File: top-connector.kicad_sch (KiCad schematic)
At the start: 6 parts, among them J1 Compute-Module-4_Plug_Connect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, Q2 DMG1012T-7

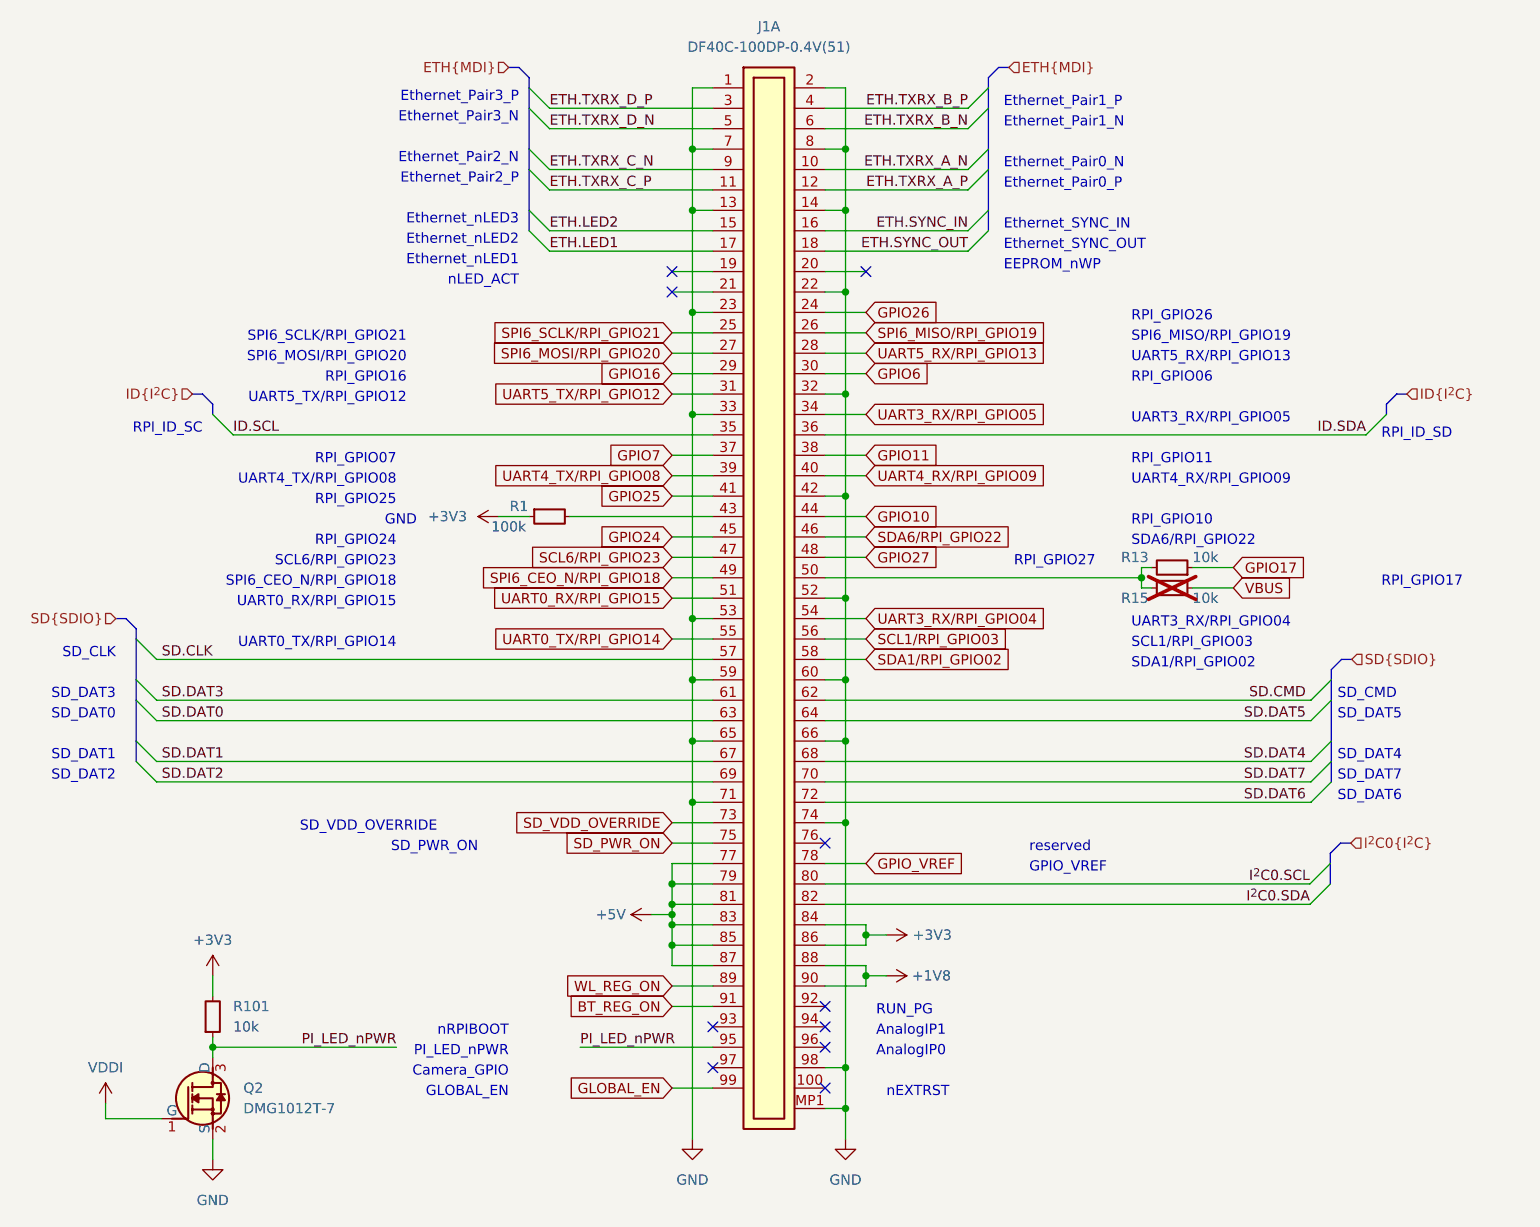
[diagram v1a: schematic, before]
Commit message: [#59450] Remove custom CM4 connector, add CM4 outline with regular DF40C-100DP-0.4V(51) connectors
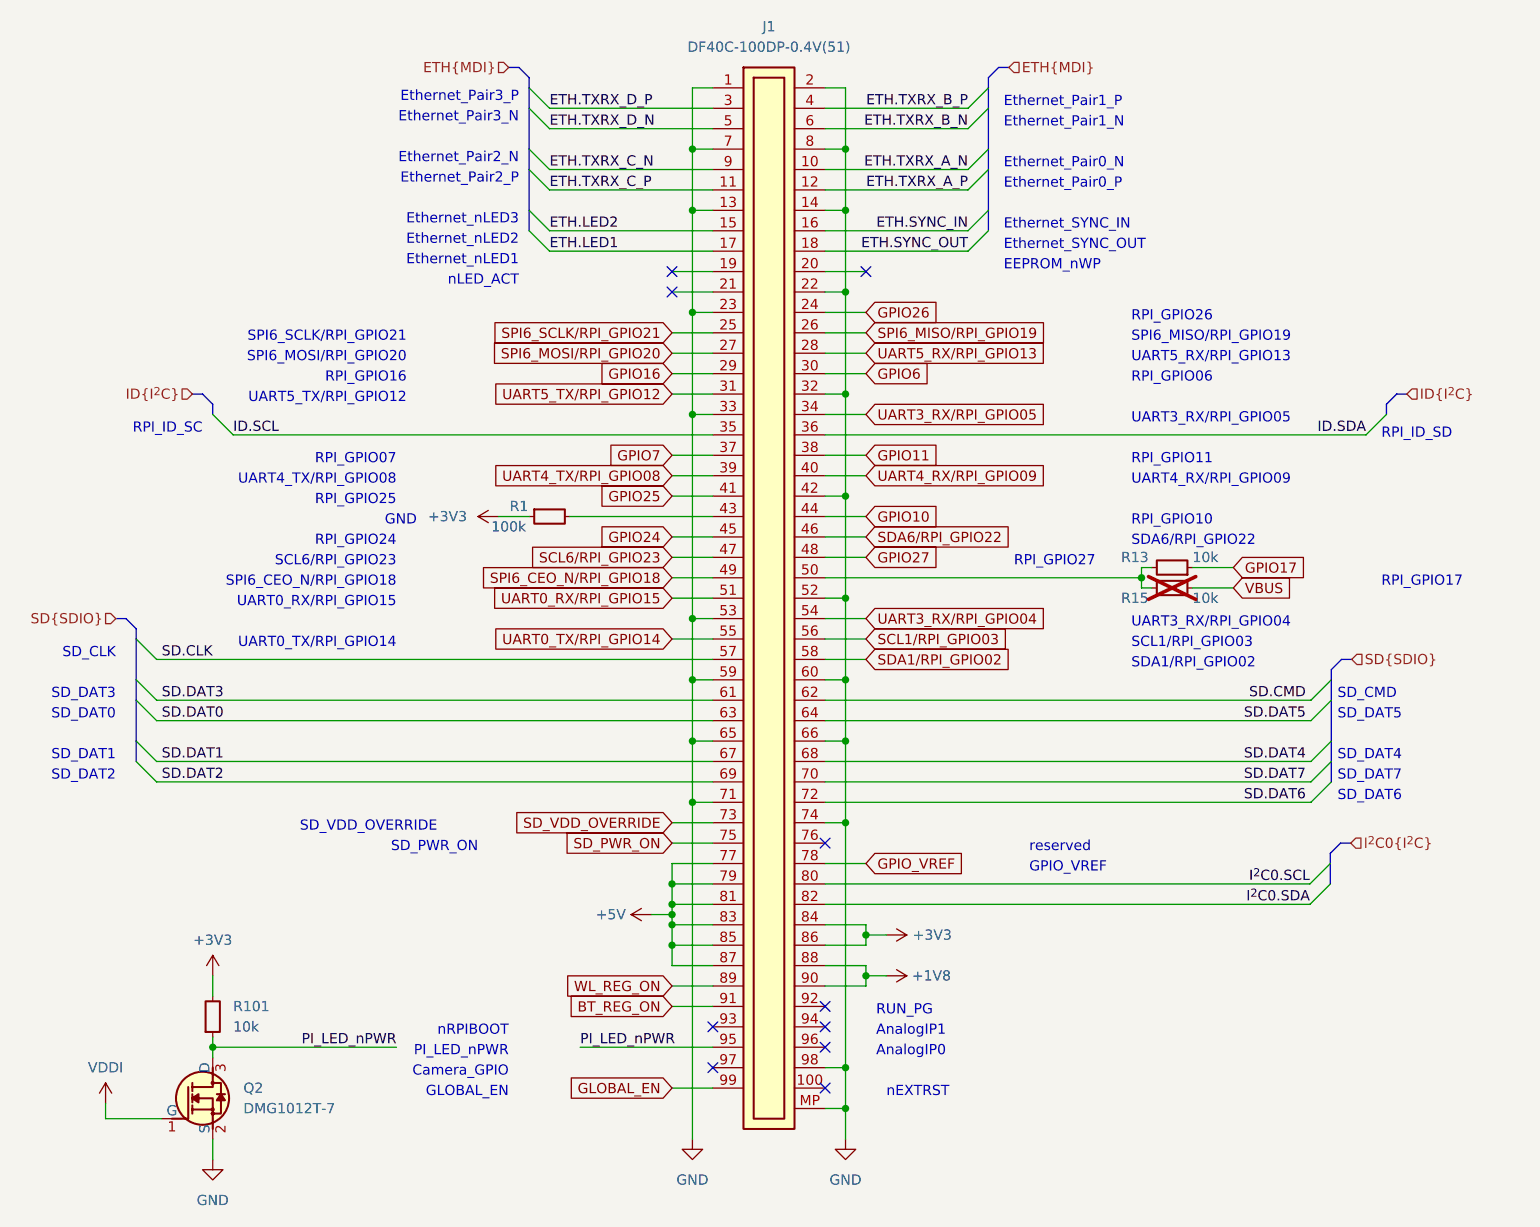
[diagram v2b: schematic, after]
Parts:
- removed J1: Compute-Module-4_Plug_Connector, antmicro-footprints:Compute-Module-4_Plug_Connector, symbol antmicroModules:Compute-Module-4_Plug_Connector
- added J1: Plug_Hirose_DF40_2x50_DF40C-100DP-0.4V, antmicro-footprints:Conn_Plug_Hirose_DF40_2x50_DF40C-100DP-0.4V, symbol antmicroB2BConnectors:Plug_Hirose_DF40_2x50_DF40C-100DP-0.4V
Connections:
- net +1V8: now also J1.88, J1.90
- net +3V3: now also J1.84, J1.86
- net +5V: now also J1.77, J1.79, J1.81, J1.83, J1.85, J1.87
- net BT_REG_ON: now also J1.91
- net ETH.LED1: now also J1.17
- net ETH.LED2: now also J1.15
- net ETH.SYNC_IN: now also J1.16
- net ETH.SYNC_OUT: now also J1.18
- net ETH.TXRX_A_N: now also J1.10
- net ETH.TXRX_A_P: now also J1.12
- net ETH.TXRX_B_N: now also J1.6
- net ETH.TXRX_B_P: now also J1.4
- net ETH.TXRX_C_N: now also J1.9
- net ETH.TXRX_C_P: now also J1.11
- net ETH.TXRX_D_N: now also J1.5
- net ETH.TXRX_D_P: now also J1.3
- net GLOBAL_EN: now also J1.99
- net GND: now also J1.1, J1.13, J1.14, J1.2, J1.22, J1.23, J1.32, J1.33, J1.42, J1.52, J1.53, J1.59, J1.60, J1.65, J1.66, J1.7, J1.71, J1.74, J1.8, J1.98, J1.MP
- net GPIO10: now also J1.44
- net GPIO11: now also J1.38
- net GPIO16: now also J1.29
- net GPIO24: now also J1.45
- net GPIO25: now also J1.41
- net GPIO26: now also J1.24
- net GPIO27: now also J1.48
- net GPIO6: now also J1.30
- net GPIO7: now also J1.37
- net GPIO_VREF: now also J1.78
- net ID.SCL: now also J1.35
- net ID.SDA: now also J1.36
- net I^{2}C0.SCL: now also J1.80
- net I^{2}C0.SDA: now also J1.82
- net PI_LED_nPWR: now also J1.95
- net SCL1/RPI_GPIO03: now also J1.56
- net SCL6/RPI_GPIO23: now also J1.47
- net SD.CLK: now also J1.57
- net SD.CMD: now also J1.62
- net SD.DAT0: now also J1.63
- net SD.DAT1: now also J1.67
- net SD.DAT2: now also J1.69
- net SD.DAT3: now also J1.61
- net SD.DAT4: now also J1.68
- net SD.DAT5: now also J1.64
- net SD.DAT6: now also J1.72
- net SD.DAT7: now also J1.70
- net SDA1/RPI_GPIO02: now also J1.58
- net SDA6/RPI_GPIO22: now also J1.46
- net SD_PWR_ON: now also J1.75
- net SD_VDD_OVERRIDE: now also J1.73
- net SPI6_CEO_N/RPI_GPIO18: now also J1.49
- net SPI6_MISO/RPI_GPIO19: now also J1.26
- net SPI6_MOSI/RPI_GPIO20: now also J1.27
- net SPI6_SCLK/RPI_GPIO21: now also J1.25
- net UART0_RX/RPI_GPIO15: now also J1.51
- net UART0_TX/RPI_GPIO14: now also J1.55
- net UART3_RX/RPI_GPIO04: now also J1.54
- net UART3_RX/RPI_GPIO05: now also J1.34
- net UART4_RX/RPI_GPIO09: now also J1.40
- net UART4_TX/RPI_GPIO08: now also J1.39
- net UART5_RX/RPI_GPIO13: now also J1.28
- net UART5_TX/RPI_GPIO12: now also J1.31
- net WL_REG_ON: now also J1.89
- net at R1.2: now also J1.43
- net at R13.2, R15.2: now also J1.50
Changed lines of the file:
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@@
+    )
+  )
+  (symbol (lib_id "antmicroB2BConnectors:Plug_Hirose_DF40_2x50_DF40C-100DP-0.4V") (at 201.93 77.47 0) (unit 1)
+    (in_bom yes) (on_board yes) (dnp no) (fields_autoplaced)
+    (property "Reference" "J1" (at 208.915 69.85 0)
+      (effects (font (size 1.27 1.27) (thickness 0.15)))
+    )
+    (property "Value" "Plug_Hirose_DF40_2x50_DF40C-100DP-0.4V" (at 238.76 82.55 0)
+      (effects (font (size 1.27 1.27) (thickness 0.15)) (justify left bottom) hide)
+    )
+    (property "Footprint" "antmicro-footprints:Conn_Plug_Hirose_DF40_2x50_DF40C-100DP-0.4V" (at 238.76 85.09 0)
+      (effects (font (size 1.27 1.27) (thickness 0.15)) (justify left bottom) hide)
+    )
+    (property "Datasheet" "https://www.hirose.com/en/product/document?clcode=CL0684-4032-1-51&productname=DF40C-100DP-0.4V(51)&series=DF40&documenttype=2DDrawing&lang=en&documentid=0001001212" (at 238.76 87.63 0)
+      (effects (font (size 1.27 1.27) (thickness 0.15)) (justify left bottom) hide)
+    )
+    (property "MPN" "DF40C-100DP-0.4V(51)" (at 208.915 72.39 0)
+      (effects (font (size 1.27 1.27) (thickness 0.15)))
+    )
+    (property "Manufacturer" "Hirose Electric" (at 238.76 90.17 0)
+      (effects (font (size 1.27 1.27) (thickness 0.15)) (justify left bottom) hide)
+    )
+    (property "Pitch" "0.4 mm" (at 238.76 92.71 0)
+      (effects (font (size 1.27 1.27)) (justify left bottom) hide)
+    )
+    (property "Author" "Antmicro" (at 238.76 95.25 0)
+      (effects (font (size 1.27 1.27) (thickness 0.15)) (justify left bottom) hide)
+    )
+    (property "License" "Apache-2.0" (at 238.76 97.79 0)
+      (effects (font (size 1.27 1.27) (thickness 0.15)) (justify left bottom) hide)
+    )
+    (pin "53")
+    (pin "57")
+    (pin "89")
+    (pin "25")
+    (pin "67")
+    (pin "27")
+    (pin "56")
+    (pin "79")
+    (pin "29")
+    (pin "43")
+    (pin "93")
+    (pin "10")
+    (pin "20")
+    (pin "19")
+    (pin "41")
+    (pin "11")
+    (pin "100")
+    (pin "13")
+    (pin "18")
+    (pin "40")
+    (pin "12")
+    (pin "1")
+    (pin "22")
+    (pin "17")
+    (pin "80")
+    (pin "64")
+    (pin "26")
+    (pin "6")
+    (pin "87")
+    (pin "3")
+    (pin "52")
+    (pin "35")
+    (pin "55")
+    (pin "94")
+    (pin "76")
+    (pin "5")
+    (pin "73")
+    (pin "71")
+    (pin "47")
+    (pin "88")
+    (pin "95")
+    (pin "14")
+    (pin "MP")
+    (pin "99")
+    (pin "85")
+    (pin "84")
+    (pin "86")
+    (pin "24")
+    (pin "59")
+    (pin "90")
+    (pin "77")
+    (pin "78")
+    (pin "69")
+    (pin "65")
+    (pin "68")
+    (pin "74")
+    (pin "60")
+    (pin "72")
+    (pin "98")
+    (pin "66")
+    (pin "45")
+    (pin "58")
+    (pin "50")
+    (pin "61")
+    (pin "62")
+    (pin "44")
+    (pin "82")
+    (pin "2")
+    (pin "96")
+    (pin "42")
+    (pin "81")
+    (pin "63")
+    (pin "97")
+    (pin "15")
+    (pin "16")
+    (pin "21")
+    (pin "36")
+    (pin "38")
+    (pin "75")
+    (pin "70")
+    (pin "8")
+    (pin "9")
+    (pin "92")
+    (pin "32")
+    (pin "31")
+    (pin "39")
+    (pin "33")
+    (pin "51")
+    (pin "4")
+    (pin "54")
+    (pin "34")
+    (pin "37")
+    (pin "28")
+    (pin "30")
+    (pin "91")
+    (pin "23")
+    (pin "48")
+    (pin "83")
+    (pin "7")
+    (pin "49")
+    (pin "46")
+    (instances
+      (project "polarfire-som"
+        (path "/db4a0d3e-2eb3-499e-977d-6eb378cfd3ed/debae449-a92d-4184-817e-09f6daf3da7c"
+          (reference "J1") (unit 1)
+        )
+      )
     )
   )
@@
         )
       )
-    )
-  )
-  (symbol (lib_id "antmicroModules:Compute-Module-4_Plug_Connector") (at 201.93 77.47 0) (unit 1)
-    (in_bom yes) (on_board yes) (dnp no) (fields_autoplaced)
-    (property "Reference" "J1" (at 208.915 69.85 0)
-      (effects (font (size 1.27 1.27) (thickness 0.15)))
-    )
-    (property "Value" "Compute-Module-4_Plug_Connector" (at 224.79 80.645 0)
-      (effects (font (size 1.27 1.27) (thickness 0.15)) (justify left bottom) hide)
-    )
-    (property "Footprint" "antmicro-footprints:Compute-Module-4_Plug_Connector" (at 224.79 83.185 0)
-      (effects (font (size 1.27 1.27) (thickness 0.15)) (justify left bottom) hide)
-    )
-    (property "Datasheet" "https://www.hirose.com/en/product/document?clcode=CL0684-4032-1-51&productname=DF40C-100DP-0.4V(51)&series=DF40&documenttype=2DDrawing&lang=en&documentid=0001001212" (at 224.79 85.725 0)
-      (effects (font (size 1.27 1.27) (thickness 0.15)) (justify left bottom) hide)
-    )
-    (property "MPN" "DF40C-100DP-0.4V(51)" (at 208.915 72.39 0)
-      (effects (font (size 1.27 1.27) (thickness 0.15)))
-    )
-    (property "Manufacturer" "Hirose Electric" (at 224.79 88.265 0)
-      (effects (font (size 1.27 1.27) (thickness 0.15)) (justify left bottom) hide)
-    )
-    (property "Pitch" "0.4 mm" (at 224.79 90.805 0)
-      (effects (font (size 1.27 1.27)) (justify left bottom) hide)
-    )
-    (property "Author" "Antmicro" (at 224.79 93.345 0)
-      (effects (font (size 1.27 1.27) (thickness 0.15)) (justify left bottom) hide)
-    )
-    (property "License" "Apache-2.0" (at 224.79 95.885 0)
-      (effects (font (size 1.27 1.27) (thickness 0.15)) (justify left bottom) hide)
-    )
-    (pin "1")
-    (pin "10")
-    (pin "100")
-    (pin "11")
-    (pin "12")
-    (pin "13")
-    (pin "14")
-    (pin "15")
-    (pin "16")
-    (pin "17")
-    (pin "18")
-    (pin "19")
-    (pin "2")
-    (pin "20")
-    (pin "21")
-    (pin "22")
-    (pin "23")
-    (pin "24")
-    (pin "25")
-    (pin "26")
-    (pin "27")
-    (pin "28")
-    (pin "29")
-    (pin "3")
-    (pin "30")
-    (pin "31")
-    (pin "32")
-    (pin "33")
-    (pin "34")
-    (pin "35")
-    (pin "36")
-    (pin "37")
-    (pin "38")
-    (pin "39")
-    (pin "4")
-    (pin "40")
-    (pin "41")
-    (pin "42")
-    (pin "43")
-    (pin "44")
-    (pin "45")
-    (pin "46")
-    (pin "47")
-    (pin "48")
-    (pin "49")
-    (pin "5")
-    (pin "50")
-    (pin "51")
-    (pin "52")
-    (pin "53")
-    (pin "54")
-    (pin "55")
-    (pin "56")
-    (pin "57")
-    (pin "58")
-    (pin "59")
-    (pin "6")
-    (pin "60")
-    (pin "61")
-    (pin "62")
-    (pin "63")
-    (pin "64")
-    (pin "65")
-    (pin "66")
-    (pin "67")
-    (pin "68")
-    (pin "69")
-    (pin "7")
-    (pin "70")
-    (pin "71")
-    (pin "72")
-    (pin "73")
-    (pin "74")
-    (pin "75")
-    (pin "76")
-    (pin "77")
-    (pin "78")
-    (pin "79")
-    (pin "8")
-    (pin "80")
-    (pin "81")
-    (pin "82")
-    (pin "83")
-    (pin "84")
-    (pin "85")
-    (pin "86")
-    (pin "87")
-    (pin "88")
-    (pin "89")
-    (pin "9")
-    (pin "90")
-    (pin "91")
-    (pin "92")
-    (pin "93")
-    (pin "94")
-    (pin "95")
-    (pin "96")
-    (pin "97")
-    (pin "98")
-    (pin "99")
-    (pin "MP1")
-    (pin "101")
-    (pin "102")
-    (pin "103")
-    (pin "104")
-    (pin "105")
-    (pin "106")
-    (pin "107")
-    (pin "108")
-    (pin "109")
-    (pin "110")
-    (pin "111")
-    (pin "112")
-    (pin "113")
-    (pin "114")
-    (pin "115")
-    (pin "116")
-    (pin "117")
-    (pin "118")
-    (pin "119")
-    (pin "120")
-    (pin "121")
-    (pin "122")
-    (pin "123")
-    (pin "124")
-    (pin "125")
-    (pin "126")
-    (pin "127")
-    (pin "128")
-    (pin "129")
-    (pin "130")
-    (pin "131")
-    (pin "132")
-    (pin "133")
-    (pin "134")
-    (pin "135")
-    (pin "136")
-    (pin "137")
-    (pin "138")
-    (pin "139")
-    (pin "140")
-    (pin "141")
-    (pin "142")
-    (pin "143")
-    (pin "144")
-    (pin "145")
-    (pin "146")
-    (pin "147")
-    (pin "148")
-    (pin "149")
-    (pin "150")
-    (pin "151")
-    (pin "152")
-    (pin "153")
-    (pin "154")
-    (pin "155")
-    (pin "156")
-    (pin "157")
-    (pin "158")
-    (pin "159")
-    (pin "160")
-    (pin "161")
-    (pin "162")
-    (pin "163")
-    (pin "164")
-    (pin "165")
-    (pin "166")
-    (pin "167")
-    (pin "168")
-    (pin "169")
-    (pin "170")
-    (pin "171")
-    (pin "172")
-    (pin "173")
-    (pin "174")
-    (pin "175")
-    (pin "176")
-    (pin "177")
-    (pin "178")
-    (pin "179")
-    (pin "180")
-    (pin "181")
-    (pin "182")
-    (pin "183")
-    (pin "184")
-    (pin "185")
-    (pin "186")
-    (pin "187")
-    (pin "188")
-    (pin "189")
-    (pin "190")
-    (pin "191")
-    (pin "192")
-    (pin "193")
-    (pin "194")
-    (pin "195")
-    (pin "196")
-    (pin "197")
-    (pin "198")
-    (pin "199")
-    (pin "200")
-    (pin "MP2")
-    (instances
-      (project "polarfire-som"
-        (path "/db4a0d3e-2eb3-499e-977d-6eb378cfd3ed/debae449-a92d-4184-817e-09f6daf3da7c"
-          (reference "J1") (unit 1)
-        )
-      )
